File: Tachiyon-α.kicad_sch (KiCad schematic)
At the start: 30 parts, among them J1 USB_B_Micro, J2 Conn_01x04_Pin, J3 Conn_01x10_Pin, J4 Conn_01x10_Pin, U1 MSPM0C1xxx/L1xxx_20pin, U2 AMS1117-3.3, U3 USBLC6-4SC6, U4 CH340N

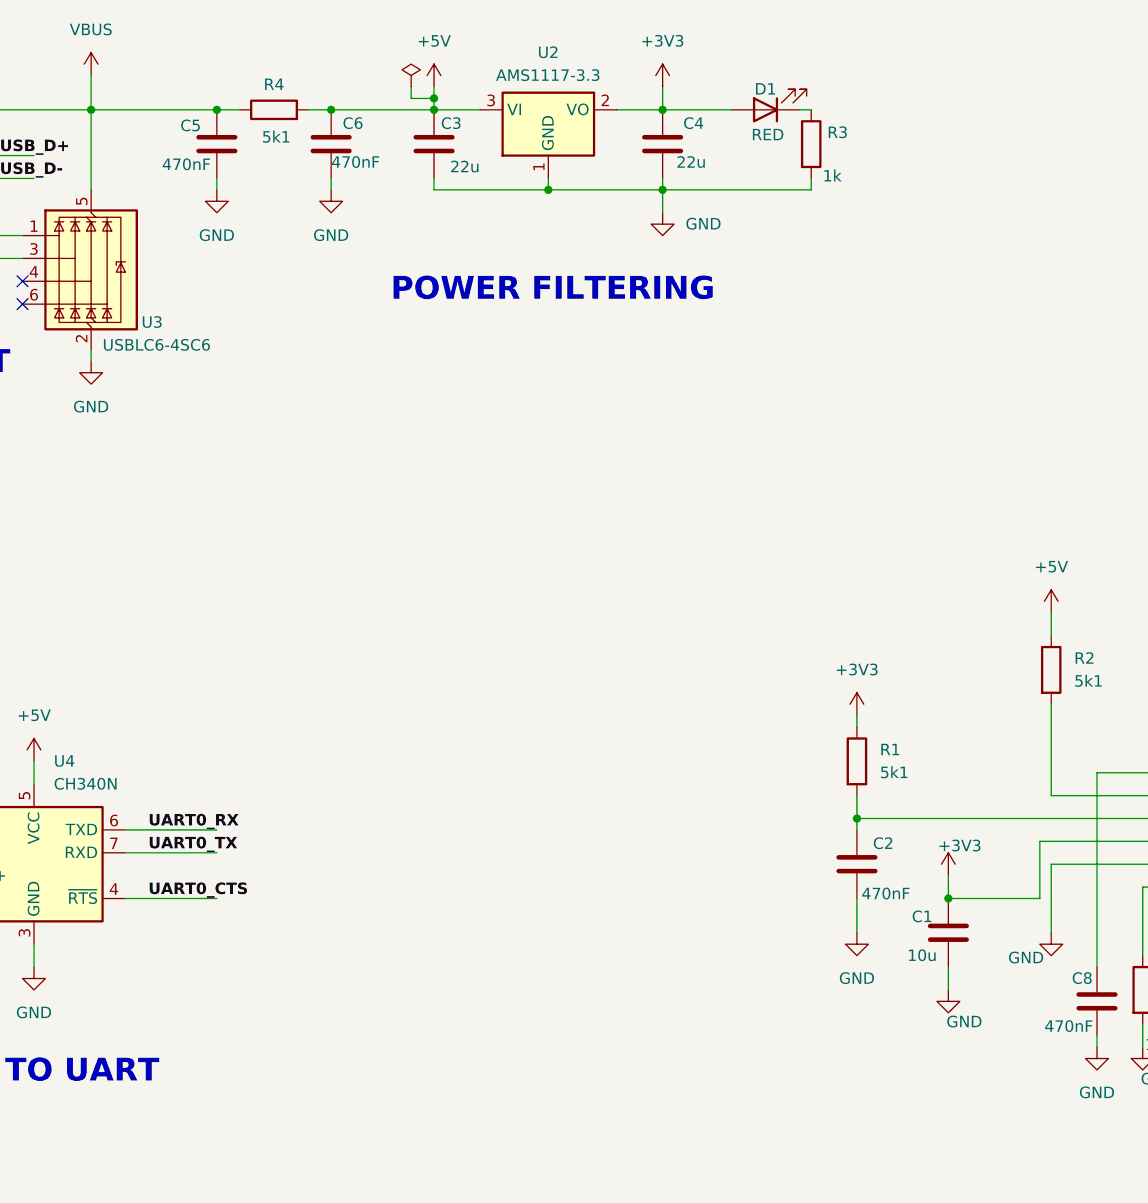
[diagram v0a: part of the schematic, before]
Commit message: Modify AMS1117 Power Input Filter Stage
- Remove Pi Filter at AMS1117 input stage and
  add a ferrite bead for EMI suppression
- Reduce Input and output stability capacitor value of AMS1117
  from 22uF to 10uF to accomodate USB2.0 bus capacitance requirements
- Modify PCB design to incorporate schematic changes
- Generate gerber files for new PCB Layout

Signed-off-by: u592003sd <sarvadnyasonic@gmail.com>
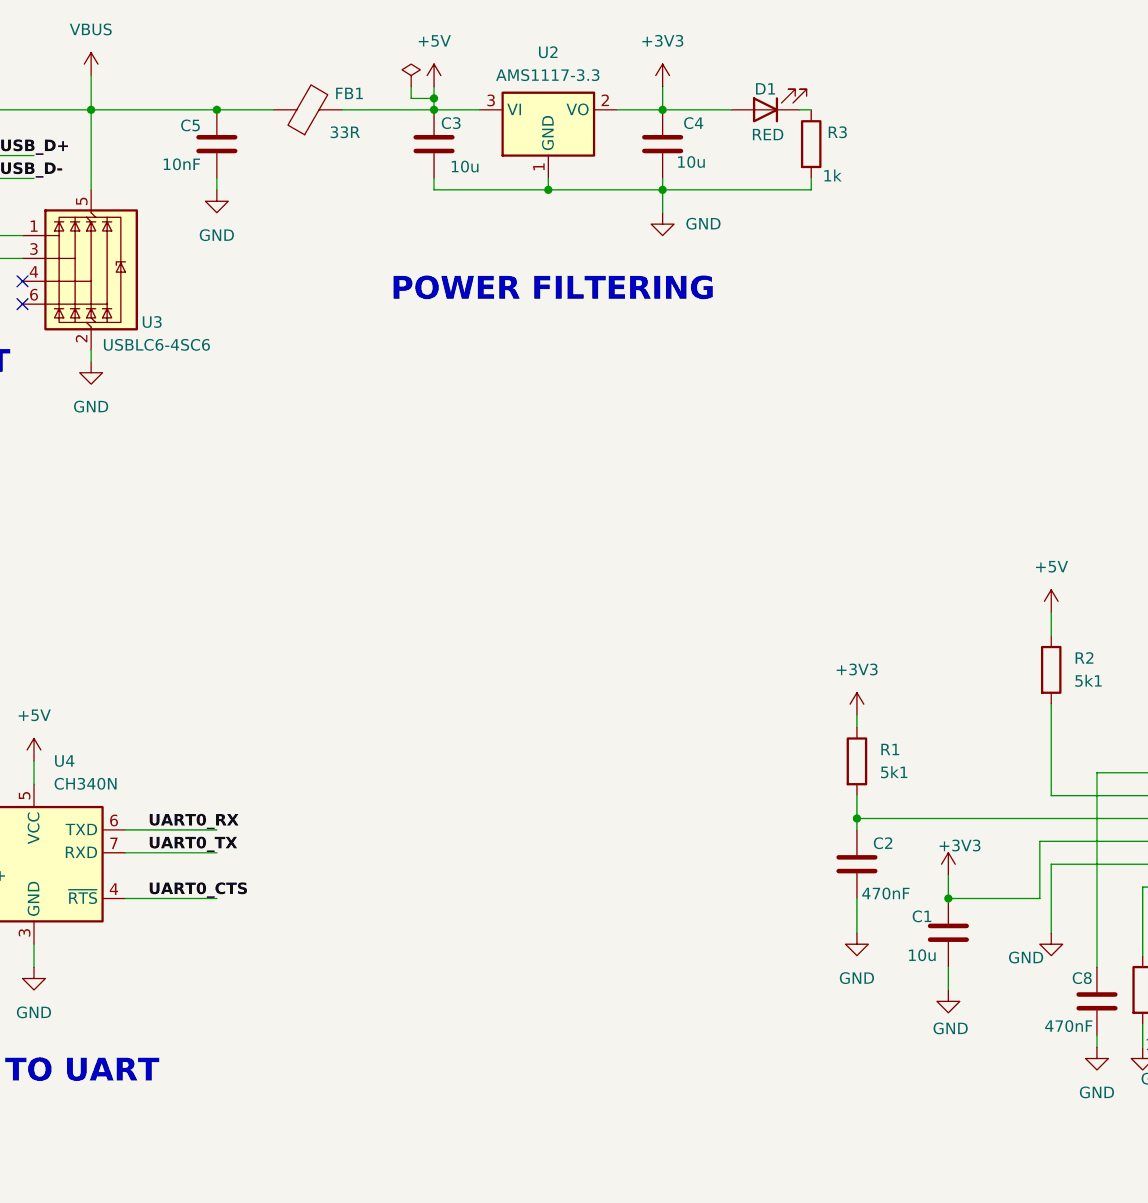
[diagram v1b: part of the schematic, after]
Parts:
- removed C6: 470nF, Capacitor_SMD:C_0603_1608Metric, symbol Device:C
- removed R4: 5k1, Resistor_SMD:R_0603_1608Metric, symbol Device:R
- added FB1: 33R, Resistor_SMD:R_0603_1608Metric, symbol Device:FerriteBead
- C3, C4: value 22u -> 10u
- C5: value 470nF -> 10nF
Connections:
- net +5V: now also FB1.2
- net VBUS: now also FB1.1
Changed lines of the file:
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@@
 	)
 	(junction
-		(at 78.74 25.4)
-		(diameter 0)
-		(color 0 0 0 0)
-	)
-	(junction
 		(at 22.86 41.91)
 		(diameter 0)
@@
 	(wire
 		(pts
-			(xy 66.04 25.4) (xy 68.58 25.4)
+			(xy 66.04 25.4) (xy 72.39 25.4)
 		)
 		(stroke
@@
 	(wire
 		(pts
-			(xy 78.74 25.4) (xy 90.17 25.4)
-		)
-		(stroke
-			(width 0)
-			(type default)
-		)
-	)
-	(wire
-		(pts
 			(xy 22.86 40.64) (xy 22.86 41.91)
 		)
@@
 	(wire
 		(pts
-			(xy 76.2 25.4) (xy 78.74 25.4)
+			(xy 80.01 25.4) (xy 90.17 25.4)
 		)
 		(stroke
@@
 	(wire
 		(pts
-			(xy 78.74 33.02) (xy 78.74 34.29)
-		)
-		(stroke
-			(width 0)
-			(type default)
-		)
-	)
-	(wire
-		(pts
 			(xy 38.1 41.91) (xy 38.1 33.02)
 		)
@@
 	)
 	(symbol
+		(lib_id "Device:FerriteBead")
+		(at 76.2 25.4 90)
+		(unit 1)
+		(exclude_from_sim no)
+		(in_bom yes)
+		(on_board yes)
+		(dnp no)
+		(property "Reference" "FB1"
+			(at 80.772 23.622 90)
+			(effects
+				(font
+					(size 1.27 1.27)
+				)
+			)
+		)
+		(property "Value" "33R"
+			(at 80.264 27.94 90)
+			(effects
+				(font
+					(size 1.27 1.27)
+				)
+			)
+		)
+		(property "Footprint" "Resistor_SMD:R_0603_1608Metric"
+			(at 76.2 27.178 90)
+			(effects
+				(font
+					(size 1.27 1.27)
+				)
+				(hide yes)
+			)
+		)
+		(property "Datasheet" "~"
+			(at 76.2 25.4 0)
+			(effects
+				(font
+					(size 1.27 1.27)
+				)
+				(hide yes)
+			)
+		)
+		(property "Description" "Ferrite bead"
+			(at 76.2 25.4 0)
+			(effects
+				(font
+					(size 1.27 1.27)
+				)
+				(hide yes)
+			)
+		)
+		(pin "1"
+		)
+		(pin "2"
+		)
+		(instances
+			(project ""
+				(path "/f86205a2-1615-4172-bff3-84d4fdd95423"
+					(reference "FB1")
+					(unit 1)
+				)
+			)
+		)
+	)
+	(symbol
 		(lib_id "power:+5V")
 		(at 90.17 22.86 0)
@@
 	)
 	(symbol
-		(lib_id "Device:R")
-		(at 72.39 25.4 90)
-		(unit 1)
-		(exclude_from_sim no)
-		(in_bom yes)
-		(on_board yes)
-		(dnp no)
-		(property "Reference" "R4"
-			(at 72.39 22.606 90)
-			(effects
-				(font
-					(size 1.27 1.27)
-				)
-			)
-		)
-		(property "Value" "5k1"
-			(at 72.644 28.448 90)
-			(effects
-				(font
-					(size 1.27 1.27)
-				)
-			)
-		)
-		(property "Footprint" "Resistor_SMD:R_0603_1608Metric"
-			(at 72.39 27.178 90)
-			(effects
-				(font
-					(size 1.27 1.27)
-				)
-				(hide yes)
-			)
-		)
-		(property "Datasheet" "~"
-			(at 72.39 25.4 0)
-			(effects
-				(font
-					(size 1.27 1.27)
-				)
-				(hide yes)
-			)
-		)
-		(property "Description" "Resistor"
-			(at 72.39 25.4 0)
-			(effects
-				(font
-					(size 1.27 1.27)
-				)
-				(hide yes)
-			)
-		)
-		(pin "1"
-		)
-		(pin "2"
-		)
-		(instances
-			(project "Tachiyon-α"
-				(path "/f86205a2-1615-4172-bff3-84d4fdd95423"
-					(reference "R4")
-					(unit 1)
-				)
-			)
-		)
-	)
-	(symbol
 		(lib_id "Connector:Conn_01x04_Pin")
 		(at 165.1 173.99 0)
@@
 		)
 		(property "Value" "GND"
-			(at 149.098 126.746 0)
+			(at 147.574 127.508 0)
 			(effects
 				(font
@@
 			)
 		)
-		(property "Value" "22u"
+		(property "Value" "10u"
 			(at 117.094 31.242 0)
 			(effects
@@
 			)
 		)
-		(property "Value" "470nF"
+		(property "Value" "10nF"
 			(at 59.944 31.496 0)
 			(effects
@@
 	)
 	(symbol
-		(lib_id "power:GND")
-		(at 78.74 34.29 0)
-		(unit 1)
-		(exclude_from_sim no)
-		(in_bom yes)
-		(on_board yes)
-		(dnp no)
-		(fields_autoplaced yes)
-		(property "Reference" "#PWR09"
-			(at 78.74 40.64 0)
-			(effects
-				(font
-					(size 1.27 1.27)
-				)
-				(hide yes)
-			)
-		)
-		(property "Value" "GND"
-			(at 78.74 39.37 0)
-			(effects
-				(font
-					(size 1.27 1.27)
-				)
-			)
-		)
-		(property "Footprint" ""
-			(at 78.74 34.29 0)
-			(effects
-				(font
-					(size 1.27 1.27)
-				)
-				(hide yes)
-			)
-		)
-		(property "Datasheet" ""
-			(at 78.74 34.29 0)
-			(effects
-				(font
-					(size 1.27 1.27)
-				)
-				(hide yes)
-			)
-		)
-		(property "Description" "Power symbol creates a global label with name \"GND\" , ground"
-			(at 78.74 34.29 0)
-			(effects
-				(font
-					(size 1.27 1.27)
-				)
-				(hide yes)
-			)
-		)
-		(pin "1"
-		)
-		(instances
-			(project "Tachiyon-α"
-				(path "/f86205a2-1615-4172-bff3-84d4fdd95423"
-					(reference "#PWR09")
-					(unit 1)
-				)
-			)
-		)
-	)
-	(symbol
 		(lib_id "power:+5V")
 		(at 45.72 97.79 0)
@@
 			)
 		)
-		(property "Value" "22u"
+		(property "Value" "10u"
 			(at 91.948 31.75 0)
 			(effects
@@
 					(unit 1)
 				)
-			)
-		)
-	)
-	(symbol
-		(lib_id "Device:C")
-		(at 78.74 29.21 0)
-		(unit 1)
-		(exclude_from_sim no)
-		(in_bom yes)
-		(on_board yes)
-		(dnp no)
-		(property "Reference" "C6"
-			(at 80.01 26.924 0)
-			(effects
-				(font
-					(size 1.27 1.27)
-				)
-				(justify left)
-			)
-		)
-		(property "Value" "470nF"
-			(at 78.74 31.242 0)
-			(effects
-				(font
-					(size 1.27 1.27)
-				)
-				(justify left)
-			)
-		)
-		(property "Footprint" "Capacitor_SMD:C_0603_1608Metric"
-			(at 79.7052 33.02 0)
-			(effects
-				(font
-					(size 1.27 1.27)
-				)
-				(hide yes)
-			)
-		)
-		(property "Datasheet" "~"
-			(at 78.74 29.21 0)
-			(effects
-				(font
-					(size 1.27 1.27)
-				)
-				(hide yes)
-			)
-		)
-		(property "Description" "Unpolarized capacitor"
-			(at 78.74 29.21 0)
-			(effects
-				(font
-					(size 1.27 1.27)
-				)
-				(hide yes)
-			)
-		)
-		(pin "1"
-		)
-		(pin "2"
-		)
-		(instances
-			(project "Tachiyon-α"
-				(path "/f86205a2-1615-4172-bff3-84d4fdd95423"
-					(reference "C6")
-					(unit 1)
-				)
